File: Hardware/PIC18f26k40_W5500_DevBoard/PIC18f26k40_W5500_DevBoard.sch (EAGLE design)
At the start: 40 parts, among them J2 MAGJACK, U1 W5500, U2 PIC18F2523-I/SO

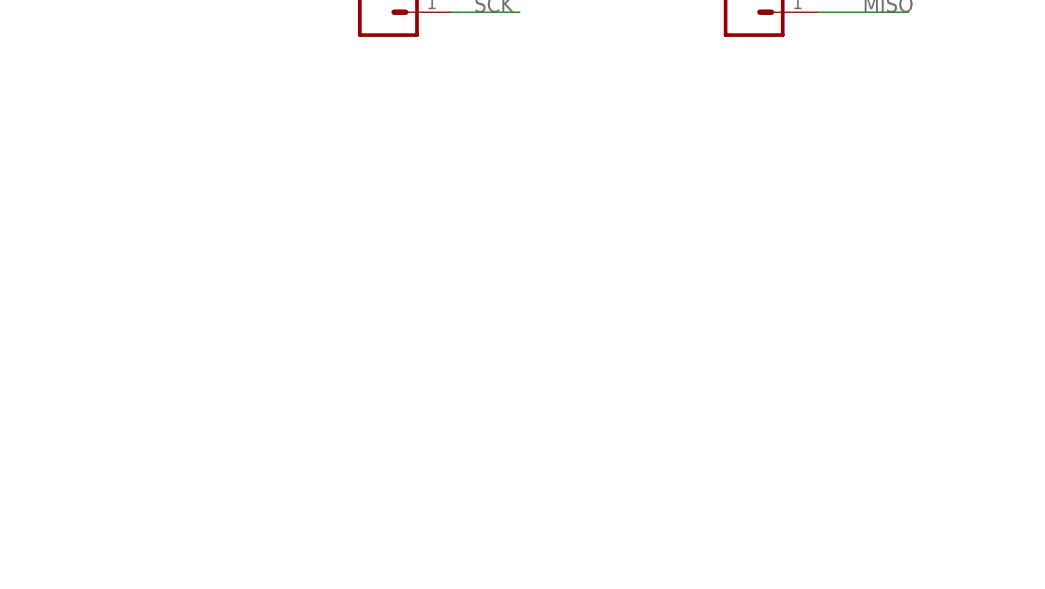
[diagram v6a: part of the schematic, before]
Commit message: #251 Added room for USB connector and voltage regulator to board
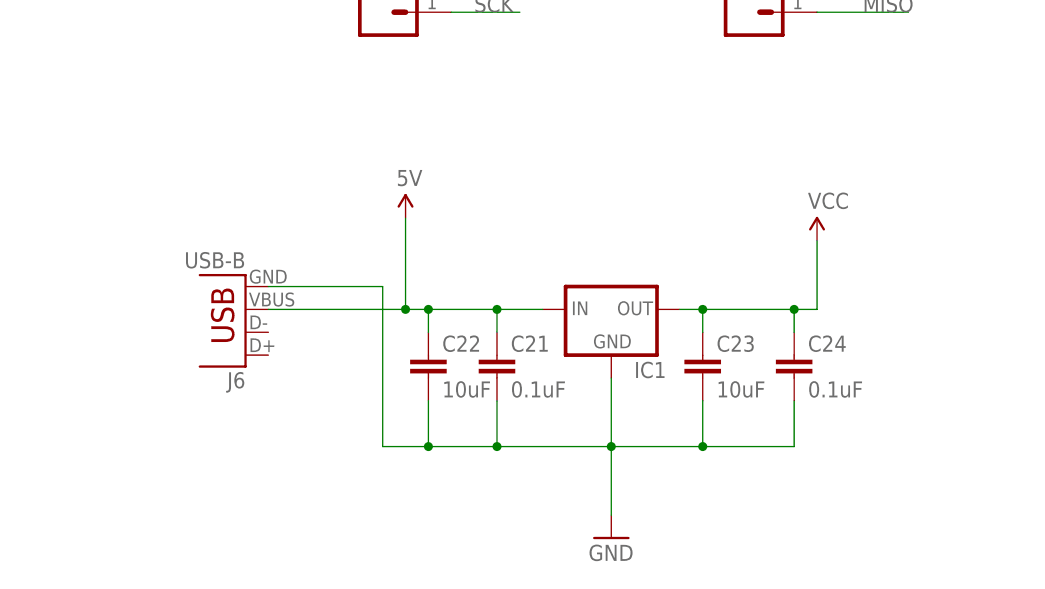
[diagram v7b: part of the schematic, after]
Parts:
- added C21, C24: 0.1uF, SparkFun-Passives:CAP0603-CAP
- added C22, C23: 10uF, SparkFun-Passives:CAP0603-CAP
- added IC1: (no value), v-reg:78XXL
- added J6: USB-B, SparkFun-Connectors:USBPTH
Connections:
- new net 5V: C21.1, C22.1, IC1.IN, J6.VBUS
- net GND: now also C21.2, C22.2, C23.2, C24.2, IC1.GND, J6.GND
- net VCC: now also C23.1, C24.1, IC1.OUT
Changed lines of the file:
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@@
 <part name="GND17" library="SparkFun-Aesthetics" deviceset="GND" device=""/>
 <part name="J5" library="SparkFun-Connectors" deviceset="M02" device="PTH"/>
+<part name="J6" library="SparkFun-Connectors" deviceset="USB" device="PTH" value="USB-B"/>
+<part name="SUPPLY12" library="SparkFun-Aesthetics" deviceset="5V" device=""/>
+<part name="IC1" library="v-reg" deviceset="78XXL" device=""/>
+<part name="SUPPLY13" library="SparkFun-Aesthetics" deviceset="VCC" device=""/>
+<part name="C21" library="SparkFun-Passives" deviceset="CAP" device="0603-CAP" value="0.1uF"/>
+<part name="C22" library="SparkFun-Passives" deviceset="CAP" device="0603-CAP" value="10uF"/>
+<part name="C23" library="SparkFun-Passives" deviceset="CAP" device="0603-CAP" value="10uF"/>
+<part name="C24" library="SparkFun-Passives" deviceset="CAP" device="0603-CAP" value="0.1uF"/>
+<part name="GND18" library="SparkFun-Aesthetics" deviceset="GND" device=""/>
 </parts>
 <sheets>
@@
 <instance part="GND17" gate="1" x="259.08" y="25.4"/>
 <instance part="J5" gate="G$1" x="297.18" y="127" rot="R180"/>
+<instance part="J6" gate="G$1" x="-5.08" y="-66.04" rot="R180"/>
+<instance part="SUPPLY12" gate="G$1" x="12.7" y="-58.42"/>
+<instance part="IC1" gate="A" x="35.56" y="-68.58"/>
+<instance part="SUPPLY13" gate="G$1" x="58.42" y="-60.96"/>
+<instance part="C21" gate="G$1" x="22.86" y="-76.2"/>
+<instance part="C22" gate="G$1" x="15.24" y="-76.2"/>
+<instance part="C23" gate="G$1" x="45.72" y="-76.2"/>
+<instance part="C24" gate="G$1" x="55.88" y="-76.2"/>
+<instance part="GND18" gate="1" x="35.56" y="-93.98"/>
 </instances>
 <busses>
@@
 <wire x1="81.28" y1="-22.86" x2="81.28" y2="-17.78" width="0.1524" layer="91"/>
 <pinref part="SUPPLY11" gate="G$1" pin="VCC"/>
+</segment>
+<segment>
+<pinref part="IC1" gate="A" pin="OUT"/>
+<wire x1="43.18" y1="-68.58" x2="45.72" y2="-68.58" width="0.1524" layer="91"/>
+<wire x1="45.72" y1="-68.58" x2="55.88" y2="-68.58" width="0.1524" layer="91"/>
+<wire x1="55.88" y1="-68.58" x2="58.42" y2="-68.58" width="0.1524" layer="91"/>
+<wire x1="58.42" y1="-68.58" x2="58.42" y2="-60.96" width="0.1524" layer="91"/>
+<pinref part="SUPPLY13" gate="G$1" pin="VCC"/>
+<pinref part="C23" gate="G$1" pin="1"/>
+<wire x1="45.72" y1="-71.12" x2="45.72" y2="-68.58" width="0.1524" layer="91"/>
+<junction x="45.72" y="-68.58"/>
+<pinref part="C24" gate="G$1" pin="1"/>
+<wire x1="55.88" y1="-71.12" x2="55.88" y2="-68.58" width="0.1524" layer="91"/>
+<junction x="55.88" y="-68.58"/>
 </segment>
 </net>
@@
 <junction x="259.08" y="27.94"/>
 </segment>
+<segment>
+<pinref part="IC1" gate="A" pin="GND"/>
+<wire x1="35.56" y1="-76.2" x2="35.56" y2="-83.82" width="0.1524" layer="91"/>
+<pinref part="C24" gate="G$1" pin="2"/>
+<wire x1="55.88" y1="-78.74" x2="55.88" y2="-83.82" width="0.1524" layer="91"/>
+<wire x1="55.88" y1="-83.82" x2="45.72" y2="-83.82" width="0.1524" layer="91"/>
+<junction x="35.56" y="-83.82"/>
+<pinref part="C23" gate="G$1" pin="2"/>
+<wire x1="45.72" y1="-83.82" x2="35.56" y2="-83.82" width="0.1524" layer="91"/>
+<wire x1="45.72" y1="-78.74" x2="45.72" y2="-83.82" width="0.1524" layer="91"/>
+<junction x="45.72" y="-83.82"/>
+<pinref part="C21" gate="G$1" pin="2"/>
+<wire x1="22.86" y1="-78.74" x2="22.86" y2="-83.82" width="0.1524" layer="91"/>
+<wire x1="22.86" y1="-83.82" x2="35.56" y2="-83.82" width="0.1524" layer="91"/>
+<pinref part="C22" gate="G$1" pin="2"/>
+<wire x1="15.24" y1="-78.74" x2="15.24" y2="-83.82" width="0.1524" layer="91"/>
+<wire x1="15.24" y1="-83.82" x2="22.86" y2="-83.82" width="0.1524" layer="91"/>
+<junction x="22.86" y="-83.82"/>
+<pinref part="J6" gate="G$1" pin="GND"/>
+<wire x1="-2.54" y1="-66.04" x2="10.16" y2="-66.04" width="0.1524" layer="91"/>
+<wire x1="10.16" y1="-66.04" x2="10.16" y2="-83.82" width="0.1524" layer="91"/>
+<wire x1="15.24" y1="-83.82" x2="10.16" y2="-83.82" width="0.1524" layer="91"/>
+<junction x="15.24" y="-83.82"/>
+<wire x1="35.56" y1="-83.82" x2="35.56" y2="-91.44" width="0.1524" layer="91"/>
+<pinref part="GND18" gate="1" pin="GND"/>
+</segment>
 </net>
 <net name="N$1" class="0">
@@
 </segment>
 </net>
+<net name="5V" class="0">
+<segment>
+<pinref part="J6" gate="G$1" pin="VBUS"/>
+<wire x1="-2.54" y1="-68.58" x2="12.7" y2="-68.58" width="0.1524" layer="91"/>
+<wire x1="12.7" y1="-68.58" x2="12.7" y2="-58.42" width="0.1524" layer="91"/>
+<pinref part="SUPPLY12" gate="G$1" pin="5V"/>
+<pinref part="IC1" gate="A" pin="IN"/>
+<wire x1="12.7" y1="-68.58" x2="15.24" y2="-68.58" width="0.1524" layer="91"/>
+<junction x="12.7" y="-68.58"/>
+<pinref part="C22" gate="G$1" pin="1"/>
+<wire x1="15.24" y1="-68.58" x2="22.86" y2="-68.58" width="0.1524" layer="91"/>
+<wire x1="22.86" y1="-68.58" x2="27.94" y2="-68.58" width="0.1524" layer="91"/>
+<wire x1="15.24" y1="-71.12" x2="15.24" y2="-68.58" width="0.1524" layer="91"/>
+<junction x="15.24" y="-68.58"/>
+<pinref part="C21" gate="G$1" pin="1"/>
+<wire x1="22.86" y1="-71.12" x2="22.86" y2="-68.58" width="0.1524" layer="91"/>
+<junction x="22.86" y="-68.58"/>
+</segment>
+</net>

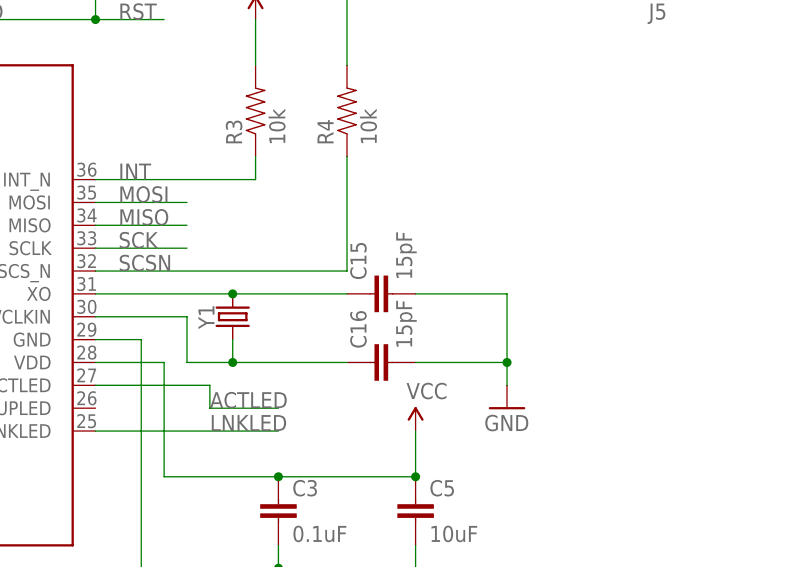
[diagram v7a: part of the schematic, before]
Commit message: #251 Fixed crystal in schematic
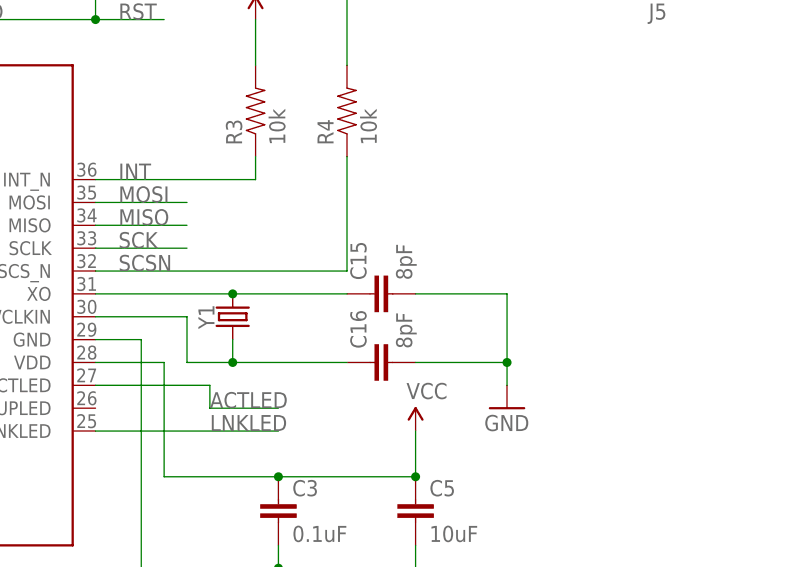
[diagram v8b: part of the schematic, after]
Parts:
- C15, C16: value 15pF -> 8pF
- Y1: device SparkFun-Clocks:CRYSTALSMD-5X3.2-4PAD -> SparkFun-Clocks:CRYSTALSMD-3.2X2.5
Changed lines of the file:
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@@
 <part name="GND9" library="SparkFun-Aesthetics" deviceset="GND" device=""/>
 <part name="SUPPLY7" library="SparkFun-Aesthetics" deviceset="VCC" device=""/>
-<part name="Y1" library="SparkFun-Clocks" deviceset="CRYSTAL" device="SMD-5X3.2-4PAD"/>
-<part name="C15" library="SparkFun-Passives" deviceset="CAP" device="0603-CAP" value="15pF"/>
-<part name="C16" library="SparkFun-Passives" deviceset="CAP" device="0603-CAP" value="15pF"/>
+<part name="C15" library="SparkFun-Passives" deviceset="CAP" device="0603-CAP" value="8pF"/>
+<part name="C16" library="SparkFun-Passives" deviceset="CAP" device="0603-CAP" value="8pF"/>
 <part name="GND10" library="SparkFun-Aesthetics" deviceset="GND" device=""/>
 <part name="SUPPLY8" library="SparkFun-Aesthetics" deviceset="VCC" device=""/>
@@
 <part name="C24" library="SparkFun-Passives" deviceset="CAP" device="0603-CAP" value="0.1uF"/>
 <part name="GND18" library="SparkFun-Aesthetics" deviceset="GND" device=""/>
+<part name="Y1" library="SparkFun-Clocks" deviceset="CRYSTAL" device="SMD-3.2X2.5"/>
 </parts>
 <sheets>
@@
 <instance part="GND9" gate="1" x="185.42" y="121.92"/>
 <instance part="SUPPLY7" gate="G$1" x="200.66" y="134.62"/>
-<instance part="Y1" gate="G$1" x="251.46" y="86.36" rot="R90"/>
 <instance part="C15" gate="G$1" x="269.24" y="88.9" rot="R90"/>
 <instance part="C16" gate="G$1" x="269.24" y="81.28" rot="R90"/>
@@
 <instance part="C24" gate="G$1" x="55.88" y="-76.2"/>
 <instance part="GND18" gate="1" x="35.56" y="-93.98"/>
+<instance part="Y1" gate="G$1" x="251.46" y="86.36" rot="R90"/>
 </instances>
 <busses>
@@
 <segment>
 <pinref part="U1" gate="G$1" pin="XO"/>
-<pinref part="Y1" gate="G$1" pin="2"/>
 <wire x1="236.22" y1="88.9" x2="251.46" y2="88.9" width="0.1524" layer="91"/>
 <pinref part="C15" gate="G$1" pin="1"/>
+<pinref part="Y1" gate="G$1" pin="2"/>
 <wire x1="251.46" y1="88.9" x2="264.16" y2="88.9" width="0.1524" layer="91"/>
 <junction x="251.46" y="88.9"/>
@@
 <wire x1="236.22" y1="86.36" x2="246.38" y2="86.36" width="0.1524" layer="91"/>
 <wire x1="246.38" y1="86.36" x2="246.38" y2="81.28" width="0.1524" layer="91"/>
-<pinref part="Y1" gate="G$1" pin="1"/>
 <wire x1="246.38" y1="81.28" x2="251.46" y2="81.28" width="0.1524" layer="91"/>
 <wire x1="251.46" y1="81.28" x2="251.46" y2="83.82" width="0.1524" layer="91"/>
@@
 <wire x1="251.46" y1="81.28" x2="264.16" y2="81.28" width="0.1524" layer="91"/>
 <junction x="251.46" y="81.28"/>
-</segment>
-</net>
+<pinref part="Y1" gate="G$1" pin="1"/>
+</segment>
+</net>
